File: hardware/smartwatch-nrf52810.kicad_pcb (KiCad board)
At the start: 4 copper layers, 46 x 46 mm, 71 parts, among them J1 J1, J2 J2, J3 J3, J4 J4, J5 J5, M1 M1, Q1 Q1, Q2 Q2, SW1 SW1, SW2 SW2, U1 NRF52810-QFAA-R, U2 BMA456, U3 HUSB238_002DD, U4 PCF8563TS/5,118, U5 BQ25180YBGR, U6 TPS63802DLAR, Y1 Y1, Y2 Y2, Y3 Y3

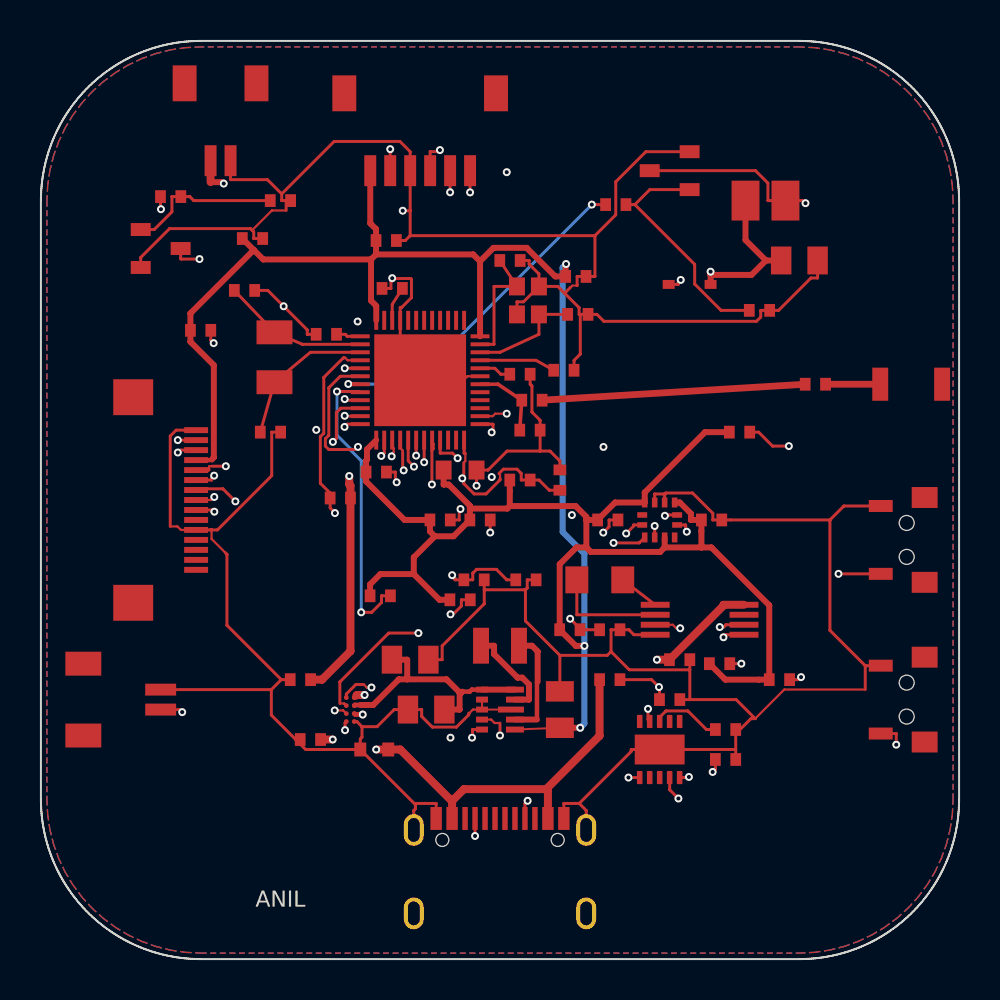
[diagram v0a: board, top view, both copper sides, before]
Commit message: Move charging port opposite centred buttons and reroute the assembly
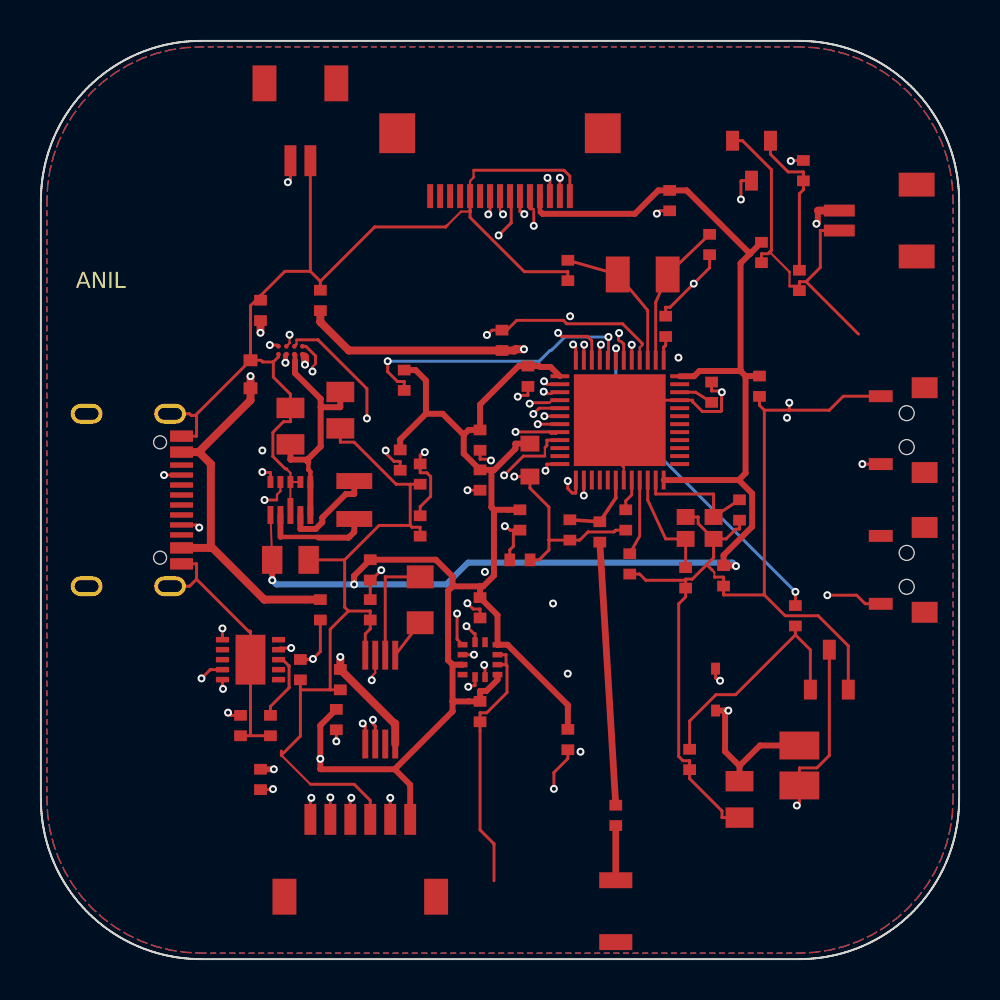
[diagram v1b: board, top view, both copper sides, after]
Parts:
- moved J3 36.6 mm to (93.0, 118.0), turned to 180 degrees
- moved J2 33.4 mm to (119.0, 86.0), turned to -90 degrees
- moved R15 31.7 mm to (115.2, 83.5), turned to -90 degrees
- moved J5 30.4 mm to (90.0, 81.0), turned to 0 degrees
- moved ANT1 30.3 mm to (105.8, 120.6), turned to -90 degrees
- moved Q1 29.9 mm to (112.6, 83.0), turned to 90 degrees
- moved M1 28.4 mm to (115.0, 113.3), turned to -90 degrees
- moved C23 27.2 mm to (112.0, 115.0), turned to -90 degrees
- moved R20 26.5 mm to (88.0, 114.0), turned to -90 degrees
- moved R16 26.3 mm to (115.0, 89.0), turned to -90 degrees
- moved Q2 26.2 mm to (116.5, 108.5), turned to -90 degrees
- moved J1 26.1 mm to (81.6, 100.0), turned to -90 degrees
- moved C15 25.5 mm to (113.1, 87.6), turned to -90 degrees
- moved R14 24.4 mm to (108.5, 85.0), turned to -90 degrees
- moved R2 24.4 mm to (87.0, 111.3), turned to -90 degrees
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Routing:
- net BUTTON2: track 43.9 -> 62.1 mm, vias 3 -> 4
- net GND: track 301.2 -> 288.5 mm
- net SWCLK: track 17.8 -> 25.7 mm, vias 2 -> 3
- net DEBUG_GPIO: track 19.5 -> 25.2 mm, vias 3 -> 2
- net BUTTON1: track 36.4 -> 41.1 mm
- net SWDIO: track 20.9 -> 25.6 mm
- net V3V0: track 151.5 -> 153.9 mm, vias 4 -> 6
- net NRST: track 24.4 -> 25.4 mm, vias 2 -> 3
